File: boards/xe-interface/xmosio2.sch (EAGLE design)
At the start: 121 parts, among them IC1 IDTQS3245QSOP20, IC2 IDTQS3245QSOP20, IC3 IDTQS3245QSOP20, IC4 IDTQS3245QSOP20, IC5 IDTQS3245QSOP20, U1 24 MHz Osc. (F535L-24), X1 0446200002

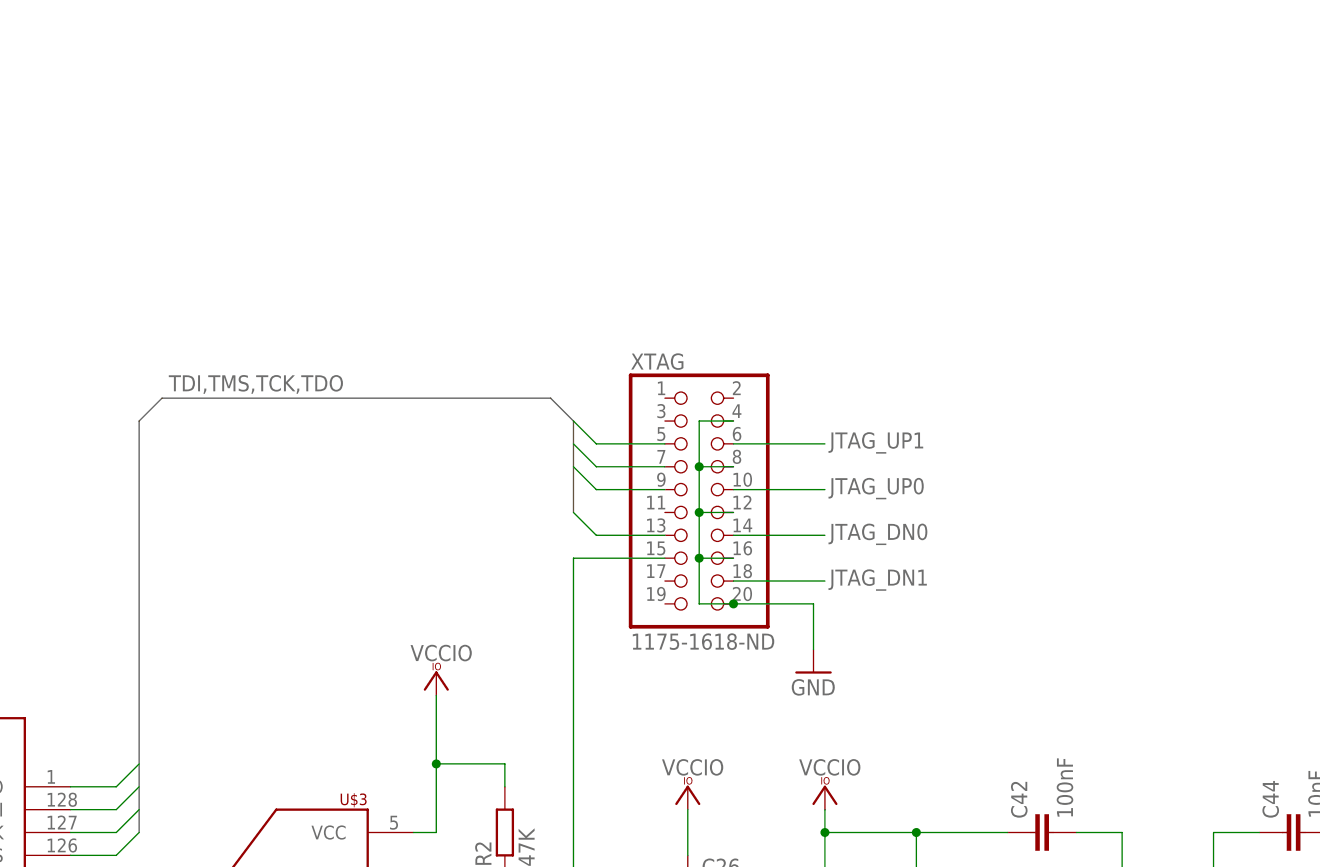
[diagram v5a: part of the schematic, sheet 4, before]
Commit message: - Fix the SD card so that the pins actually connect, even though they seem to be fine in the schematic  - Move some of the decoupling capacitors closer to the XMOS chip  - Provide JTAG +5V connection through pin header for manual selection  - Link up the 2 GPIO ports to the UART on the XTAG so they can be a serial connection during bringup  - Rotate the solder bridges on the power sections so they point the right way
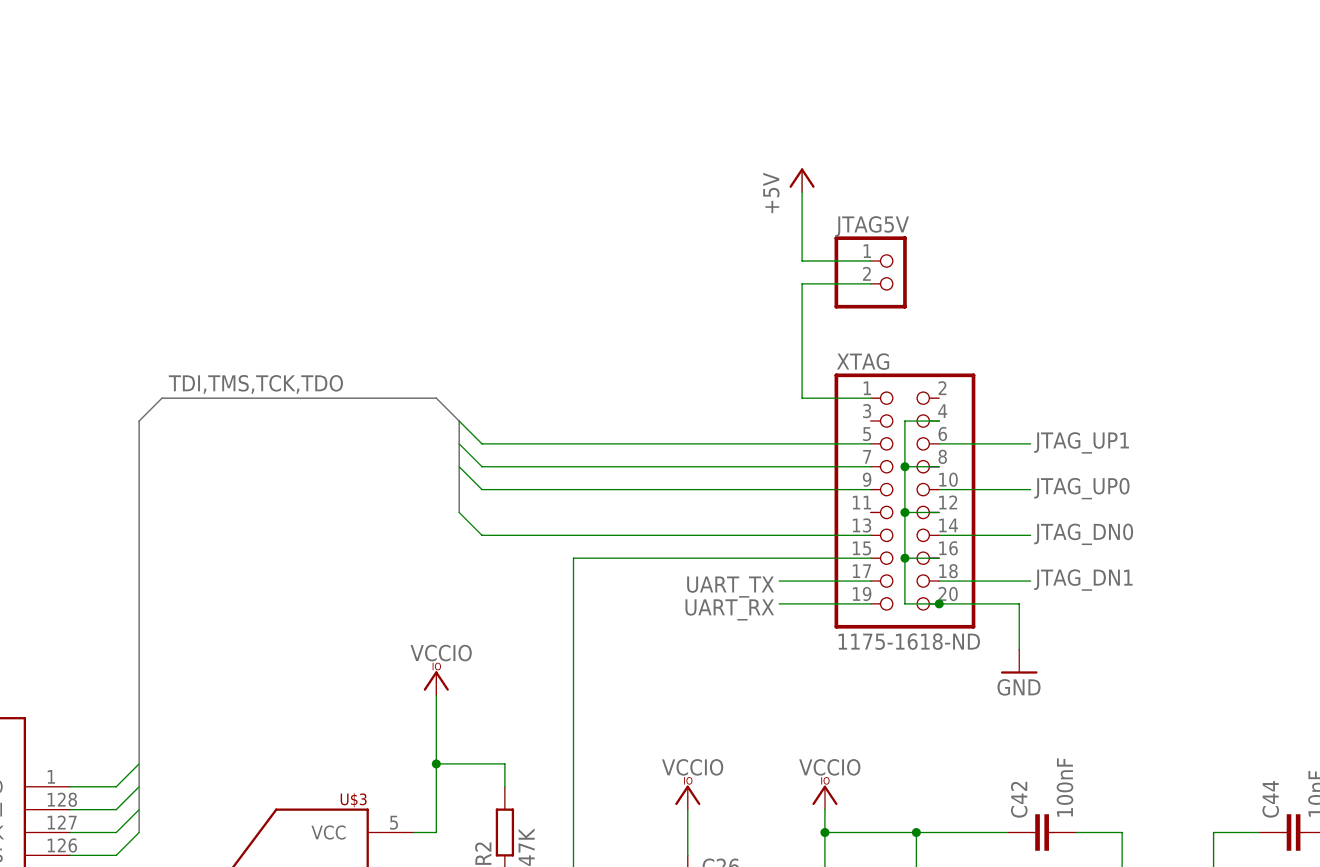
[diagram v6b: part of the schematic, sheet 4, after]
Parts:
- added JTAG5V: (no value), pinhead:PINHD-1X2
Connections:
- net N$21 renamed TRST_N
- removed net N$36: GPIO.3, U$2TILE1.X1D34@12
- removed net N$37: GPIO.2, U$2TILE1.X1D35@14
- new net N$38: JTAG5V.2, XTAG.1
- new net UART_RX: GPIO.2, U$2TILE1.X1D35@14, XTAG.19
- new net UART_TX: GPIO.3, U$2TILE1.X1D34@12, XTAG.17
- net +5V: now also JTAG5V.1
- net SDC_CD: now also J1.CD
- net SDC_CLK: now also J1.CLK
- net SDC_CMD: now also J1.CMD
- net SDC_D0: now also J1.DAT0
- net SDC_D1: now also J1.DAT1
- net SDC_D2: now also J1.DAT2
- net SDC_D3: now also J1.DAT3
- net VCCIO: now also J1.VDD
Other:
- note added: "Used as UART during bringup"
- moved on the sheet: R12, R13, XTAG

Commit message: Fix or approve all the ERC warnings in the schematic. Fix all the DRC warnings
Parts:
- GPIO: value (none) -> UART
- J1: value (none) -> SD_CARD
- JTAG5V: value (none) -> PSU
- MEM_SEL: value (none) -> CT2092MS-ND
- PBI_ID: value (none) -> CT2093MS-ND
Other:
- note removed: "CT2092MS-ND"
- note removed: "CT2093MS-ND"
- moved on the sheet: GPIO
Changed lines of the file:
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@@
 <part name="H3" library="holes" deviceset="MOUNT-HOLE" device="3.2"/>
 <part name="H4" library="holes" deviceset="MOUNT-HOLE" device="3.2"/>
-<part name="MEM_SEL" library="special" deviceset="SW_DIP-2" device=""/>
+<part name="MEM_SEL" library="special" deviceset="SW_DIP-2" device="" value="CT2092MS-ND"/>
 <part name="VCC27" library="supply1" deviceset="VCCIO" device=""/>
 <part name="R29" library="rcl" deviceset="R-EU_" device="R1206" value="10K"/>
 <part name="R30" library="rcl" deviceset="R-EU_" device="R1206" value="10K"/>
-<part name="PBI_ID" library="special" deviceset="SW_DIP-3" device=""/>
+<part name="PBI_ID" library="special" deviceset="SW_DIP-3" device="" value="CT2093MS-ND"/>
 <part name="R31" library="rcl" deviceset="R-EU_" device="R1206" value="10K"/>
 <part name="R33" library="rcl" deviceset="R-EU_" device="R1206" value="10K"/>
@@
 <part name="GND49" library="supply1" deviceset="GND" device=""/>
 <part name="P+5" library="supply1" deviceset="+5V" device=""/>
-<part name="GPIO" library="pinhead" deviceset="PINHD-1X4" device=""/>
+<part name="GPIO" library="pinhead" deviceset="PINHD-1X4" device="" value="UART"/>
 <part name="GND50" library="supply1" deviceset="GND" device=""/>
 <part name="VCC29" library="supply1" deviceset="VCCIO" device=""/>
-<part name="J1" library="InputOutputIO (rev17e)" deviceset="693063020911" device=""/>
+<part name="J1" library="InputOutputIO (rev17e)" deviceset="693063020911" device="" value="SD_CARD"/>
 <part name="VCC30" library="supply1" deviceset="VCCIO" device=""/>
 <part name="VCC31" library="supply1" deviceset="VCCIO" device=""/>
 <part name="GND51" library="supply1" deviceset="GND" device=""/>
 <part name="P+6" library="supply1" deviceset="+5V" device=""/>
-<part name="JTAG5V" library="pinhead" deviceset="PINHD-1X2" device=""/>
+<part name="JTAG5V" library="pinhead" deviceset="PINHD-1X2" device="" value="PSU"/>
 </parts>
 <sheets>
@@
 <text x="35.56" y="175.26" size="2.1844" layer="97">Use diode to get 4.3v
 from the 5v supply for QS</text>
-<text x="226.06" y="121.92" size="1.27" layer="97">CT2092MS-ND</text>
-<text x="220.98" y="86.36" size="1.27" layer="97">Used as UART
+<text x="231.14" y="66.04" size="1.27" layer="97">Used as UART
 during bringup</text>
 </plain>
@@
 <attribute name="VALUE" x="189.23" y="46.482" size="1.778" layer="96" rot="R180"/>
 </instance>
-<instance part="MEM_SEL" gate="G$1" x="233.68" y="129.54"/>
+<instance part="MEM_SEL" gate="G$1" x="233.68" y="129.54" smashed="yes">
+<attribute name="NAME" x="228.6" y="132.715" size="1.778" layer="95"/>
+<attribute name="VALUE" x="223.52" y="121.92" size="1.778" layer="96"/>
+</instance>
 <instance part="VCC27" gate="G$1" x="223.52" y="137.16" smashed="yes">
 <attribute name="VALUE" x="219.71" y="139.192" size="1.778" layer="96"/>
@@
 <instance part="GND49" gate="1" x="-2.54" y="22.86"/>
 <instance part="P+5" gate="1" x="-2.54" y="175.26"/>
-<instance part="GPIO" gate="A" x="238.76" y="88.9" rot="R180"/>
-<instance part="GND50" gate="1" x="248.92" y="76.2"/>
-<instance part="VCC29" gate="G$1" x="248.92" y="99.06" smashed="yes">
-<attribute name="VALUE" x="245.11" y="101.092" size="1.778" layer="96"/>
+<instance part="GPIO" gate="A" x="231.14" y="88.9" rot="R180"/>
+<instance part="GND50" gate="1" x="241.3" y="76.2"/>
+<instance part="VCC29" gate="G$1" x="241.3" y="99.06" smashed="yes">
+<attribute name="VALUE" x="237.49" y="101.092" size="1.778" layer="96"/>
 </instance>
 </instances>
@@
 <pinref part="GND50" gate="1" pin="GND"/>
 <pinref part="GPIO" gate="A" pin="1"/>
-<wire x1="248.92" y1="78.74" x2="248.92" y2="83.82" width="0.1524" layer="91"/>
-<wire x1="248.92" y1="83.82" x2="241.3" y2="83.82" width="0.1524" layer="91"/>
+<wire x1="241.3" y1="78.74" x2="241.3" y2="83.82" width="0.1524" layer="91"/>
+<wire x1="241.3" y1="83.82" x2="233.68" y2="83.82" width="0.1524" layer="91"/>
 </segment>
 </net>
@@
 <pinref part="GPIO" gate="A" pin="4"/>
 <pinref part="VCC29" gate="G$1" pin="VCCIO"/>
-<wire x1="241.3" y1="91.44" x2="248.92" y2="91.44" width="0.1524" layer="91"/>
-<wire x1="248.92" y1="91.44" x2="248.92" y2="96.52" width="0.1524" layer="91"/>
+<wire x1="233.68" y1="91.44" x2="241.3" y2="91.44" width="0.1524" layer="91"/>
+<wire x1="241.3" y1="91.44" x2="241.3" y2="96.52" width="0.1524" layer="91"/>
 </segment>
 </net>
@@
 <pinref part="U$2" gate="TILE1" pin="X1D34@12"/>
 <pinref part="GPIO" gate="A" pin="3"/>
-<wire x1="274.32" y1="88.9" x2="241.3" y2="88.9" width="0.1524" layer="91"/>
+<wire x1="274.32" y1="88.9" x2="233.68" y2="88.9" width="0.1524" layer="91"/>
+<label x="246.888" y="89.662" size="1.27" layer="95"/>
 </segment>
 </net>
@@
 <pinref part="U$2" gate="TILE1" pin="X1D35@14"/>
 <pinref part="GPIO" gate="A" pin="2"/>
-<wire x1="274.32" y1="86.36" x2="241.3" y2="86.36" width="0.1524" layer="91"/>
+<wire x1="274.32" y1="86.36" x2="233.68" y2="86.36" width="0.1524" layer="91"/>
+<label x="255.016" y="85.852" size="1.27" layer="95" rot="R180"/>
 </segment>
 </net>
@@
 <text x="142.24" y="-43.18" size="1.778" layer="97">Note: SDRAM byte lanes aren't supported. Do a read/modify/write to write individual bytes </text>
 <text x="127" y="-22.86" size="1.778" layer="97">W9825G6KH</text>
-<text x="199.39" y="34.29" size="1.27" layer="97" rot="R90">CT2093MS-ND</text>
 </plain>
 <instances>
@@
 <instance part="GND27" gate="1" x="93.98" y="2.54"/>
 <instance part="C35" gate="G$1" x="210.82" y="86.36"/>
-<instance part="VCC12" gate="G$1" x="198.12" y="99.06" smashed="yes">
-<attribute name="VALUE" x="202.184" y="102.108" size="1.778" layer="96" rot="R180"/>
+<instance part="VCC12" gate="G$1" x="198.12" y="104.14" smashed="yes">
+<attribute name="VALUE" x="202.184" y="107.188" size="1.778" layer="96" rot="R180"/>
 </instance>
 <instance part="GND28" gate="1" x="198.12" y="68.58"/>
@@
 <attribute name="VALUE" x="5.588" y="28.194" size="1.778" layer="96"/>
 </instance>
-<instance part="PBI_ID" gate="A" x="205.74" y="40.64" rot="R270"/>
+<instance part="PBI_ID" gate="A" x="205.74" y="40.64" smashed="yes" rot="R270">
+<attribute name="NAME" x="213.36" y="43.053" size="1.778" layer="95"/>
+<attribute name="VALUE" x="213.36" y="38.1" size="1.778" layer="96"/>
+</instance>
 <instance part="R31" gate="G$1" x="203.2" y="7.62" rot="R90"/>
 <instance part="R33" gate="G$1" x="228.6" y="7.62" rot="R90"/>
@@
 </segment>
 <segment>
-<pinref part="U$8" gate="G$2" pin="VCC"/>
-<wire x1="198.12" y1="91.44" x2="198.12" y2="93.98" width="0.1524" layer="91"/>
-<pinref part="C35" gate="G$1" pin="1"/>
-<wire x1="198.12" y1="93.98" x2="198.12" y2="96.52" width="0.1524" layer="91"/>
-<wire x1="210.82" y1="88.9" x2="210.82" y2="93.98" width="0.1524" layer="91"/>
-<wire x1="210.82" y1="93.98" x2="198.12" y2="93.98" width="0.1524" layer="91"/>
-<junction x="198.12" y="93.98"/>
-<pinref part="VCC12" gate="G$1" pin="VCCIO"/>
-<wire x1="198.12" y1="96.52" x2="198.12" y2="99.06" width="0.1524" layer="91"/>
-</segment>
-<segment>
 <pinref part="VCC13" gate="G$1" pin="VCCIO"/>
 <pinref part="C36" gate="G$1" pin="1"/>
@@
 <wire x1="203.2" y1="53.34" x2="203.2" y2="48.26" width="0.1524" layer="91"/>
 </segment>
+<segment>
+<pinref part="VCC12" gate="G$1" pin="VCCIO"/>
+<pinref part="U$8" gate="G$2" pin="VCC"/>
+<wire x1="198.12" y1="101.6" x2="198.12" y2="96.52" width="0.1524" layer="91"/>
+<pinref part="C35" gate="G$1" pin="1"/>
+<wire x1="198.12" y1="96.52" x2="198.12" y2="91.44" width="0.1524" layer="91"/>
+<wire x1="210.82" y1="88.9" x2="210.82" y2="96.52" width="0.1524" layer="91"/>
+<wire x1="210.82" y1="96.52" x2="198.12" y2="96.52" width="0.1524" layer="91"/>
+<junction x="198.12" y="96.52"/>
+</segment>
 </net>
 <net name="GND" class="0">
@@
 </instances>
 <busses>
-<bus name="RIN1-,RIN1+,DOUT1-,DOUT1+,RIN2-,RIN2+,DOUT2-,DOUT2+">
+<bus name="RIN1_N,RIN1_P,DOUT1_N,DOUT1_P,RIN2_N,RIN2_P,DOUT2_N,DOUT2_P">
 <segment>
 <wire x1="175.26" y1="180.34" x2="175.26" y2="218.44" width="0.762" layer="92"/>
@@
 <wire x1="203.2" y1="220.98" x2="205.74" y2="218.44" width="0.762" layer="92"/>
 <wire x1="205.74" y1="218.44" x2="205.74" y2="190.5" width="0.762" layer="92"/>
+<label x="177.8" y="223.52" size="1.27" layer="95"/>
 </segment>
 </bus>
@@
 </sheet>
 </sheets>
+<errors>
+</errors>
 </schematic>
 </drawing>

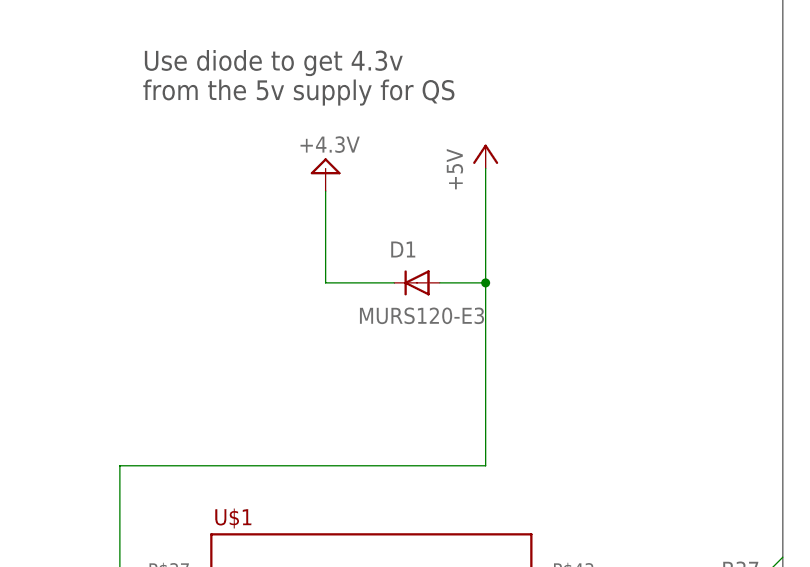
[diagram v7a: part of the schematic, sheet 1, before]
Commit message: Use a 4N4001 diode (even though it’s through-hole) because the forward voltage drop of the original one was only 0.2v, and we actually want to use the diode to drop the voltage by 0.7v.
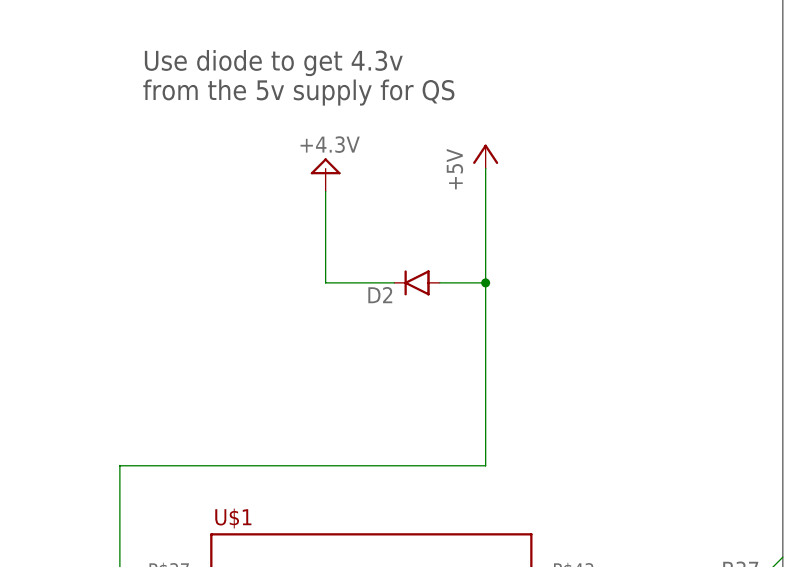
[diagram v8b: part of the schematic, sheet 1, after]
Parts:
- removed D1: MURS120-E3, diode:DIODE-SMB
- added D2: (no value), SparkFun-DiscreteSemi:DIODE
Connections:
- net +4.3V: now also D2.C; no longer D1.C
- net +5V: now also D2.A; no longer D1.A
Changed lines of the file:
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@@
 <setting verticaltext="up"/>
 </settings>
-<grid distance="0.1" unitdist="inch" unit="inch" style="lines" multiple="1" display="yes" altdistance="0.01" altunitdist="inch" altunit="inch"/>
+<grid distance="0.1" unitdist="inch" unit="inch" style="lines" multiple="1" display="no" altdistance="0.01" altunitdist="inch" altunit="inch"/>
 <layers>
 <layer number="1" name="Top" color="4" fill="1" visible="no" active="no"/>
@@
 <part name="GND9" library="supply1" deviceset="GND" device=""/>
 <part name="P+1" library="supply1" deviceset="+5V" device=""/>
-<part name="D1" library="diode" deviceset="DIODE-" device="SMB" value="MURS120-E3"/>
 <part name="GND10" library="supply1" deviceset="GND" device=""/>
 <part name="GND12" library="supply1" deviceset="GND" device=""/>
@@
 <part name="P+6" library="supply1" deviceset="+5V" device=""/>
 <part name="JTAG5V" library="pinhead" deviceset="PINHD-1X2" device="" value="PSU"/>
+<part name="D2" library="SparkFun-DiscreteSemi" deviceset="DIODE" device=""/>
 </parts>
 <sheets>
@@
 <instance part="GND9" gate="1" x="149.86" y="7.62"/>
 <instance part="P+1" gate="1" x="73.66" y="170.18"/>
-<instance part="D1" gate="G$1" x="66.04" y="154.94" smashed="yes" rot="R180">
-<attribute name="NAME" x="66.04" y="159.5374" size="1.778" layer="95" rot="R180"/>
-<attribute name="VALUE" x="73.66" y="152.1714" size="1.778" layer="96" rot="R180"/>
-</instance>
 <instance part="GND10" gate="1" x="33.02" y="10.16"/>
 <instance part="U$2" gate="TILE1" x="289.56" y="121.92" rot="MR0"/>
@@
 <attribute name="VALUE" x="237.49" y="101.092" size="1.778" layer="96"/>
 </instance>
+<instance part="D2" gate="G$1" x="66.04" y="154.94" rot="R180"/>
 </instances>
 <busses>
@@
 <wire x1="73.66" y1="154.94" x2="68.58" y2="154.94" width="0.1524" layer="91"/>
 <pinref part="P+1" gate="1" pin="+5V"/>
-<pinref part="D1" gate="G$1" pin="A"/>
 <pinref part="U$1" gate="G$1" pin="VCC5@E_7"/>
 <wire x1="38.1" y1="121.92" x2="33.02" y2="121.92" width="0.1524" layer="91"/>
@@
 <wire x1="73.66" y1="134.62" x2="73.66" y2="154.94" width="0.1524" layer="91"/>
 <junction x="73.66" y="154.94"/>
+<pinref part="D2" gate="G$1" pin="A"/>
 </segment>
 <segment>
@@
 <wire x1="63.5" y1="154.94" x2="55.88" y2="154.94" width="0.1524" layer="91"/>
 <wire x1="55.88" y1="154.94" x2="55.88" y2="165.1" width="0.1524" layer="91"/>
-<pinref part="D1" gate="G$1" pin="C"/>
 <pinref part="U$13" gate="G$1" pin="+4.3V"/>
-</segment>
-<segment>
+<pinref part="D2" gate="G$1" pin="C"/>
+</segment>
+<segment>
